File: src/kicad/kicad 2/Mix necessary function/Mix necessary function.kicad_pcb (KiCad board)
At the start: 2 copper layers, 53 x 58 mm, 22 parts, among them SW1 02-JST, SW2 02-JST

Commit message: twelite
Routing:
- net N$9: vias 1 -> 0
- net N$8: vias 1 -> 0
- net N$7: vias 1 -> 0
- net N$6: vias 1 -> 0
- net N$5: vias 1 -> 0
- net N$4: vias 1 -> 0
- net N$3: vias 1 -> 0
- net N$18: vias 1 -> 0
- net N$17: vias 1 -> 0
- net N$16: vias 1 -> 0
- net N$15: vias 1 -> 0
- net N$14: vias 1 -> 0
- net N$12: vias 1 -> 0
- net N$11: vias 1 -> 0
- net N$10: vias 1 -> 0
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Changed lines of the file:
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@@
       (outputformat 1)
       (mirror false)
-      (drillshape 1)
+      (drillshape 0)
       (scaleselection 1)
-      (outputdirectory "")
+      (outputdirectory "gerber/")
     )
   )
@@
   (net 9 "PWM2_SERVO")
   (net 10 "PWM1_SERVO")
-  (net 11 "N$1")
-  (net 12 "N$3")
-  (net 13 "N$4")
-  (net 14 "N$5")
-  (net 15 "N$6")
-  (net 16 "N$7")
-  (net 17 "N$8")
-  (net 18 "N$9")
-  (net 19 "N$10")
-  (net 20 "N$11")
-  (net 21 "N$12")
-  (net 22 "N$13")
-  (net 23 "N$14")
-  (net 24 "N$15")
-  (net 25 "N$16")
-  (net 26 "N$17")
-  (net 27 "N$18")
+  (net 11 "N$13")
   (footprint "Mix necessary function:ＮＪＭ７８０６ＦＡ-6V" (layer "F.Cu")
     (at 155.0011 100.0036 90)
@@
     (fp_line (start 10.65 -8) (end 10.65 -3.9)
       (stroke (width 0.127) (type solid)) (layer "F.SilkS"))
-    (fp_arc (start -7 2.6) (mid -9.398063 -0.328203) (end -10.65 -3.9)
+    (fp_arc (start -7 2.6) (mid -9.398061 -0.328204) (end -10.65 -3.9)
       (stroke (width 0.127) (type solid)) (layer "F.SilkS"))
     (fp_arc (start 10.65 -3.9) (mid 9.398063 -0.328203) (end 7 2.6)
@@
   (segment (start 159.145781 107.1932) (end 160.2911 108.338519) (width 0.5) (layer "F.Cu") (net 1))
   (segment (start 160.4311 120.2936) (end 160.2911 120.1536) (width 0.5) (layer "F.Cu") (net 1))
+  (via (at 137.1141 118.5266) (size 0.7564) (drill 0.35) (layers "F.Cu" "B.Cu") (net 2))
+  (via (at 169.8801 123.7336) (size 0.7564) (drill 0.35) (layers "F.Cu" "B.Cu") (net 2))
+  (via (at 155.9101 87.2216) (size 0.7564) (drill 0.35) (layers "F.Cu" "B.Cu") (net 2))
+  (via (at 144.3361 119.4146) (size 0.7564) (drill 0.35) (layers "F.Cu" "B.Cu") (net 2))
+  (via (at 162.4511 124.6066) (size 0.7564) (drill 0.35) (layers "F.Cu" "B.Cu") (net 2))
+  (via (at 146.9401 131.6406) (size 0.7564) (drill 0.35) (layers "F.Cu" "B.Cu") (free) (net 2))
+  (via (at 154.1001 107.7326) (size 0.7564) (drill 0.35) (layers "F.Cu" "B.Cu") (net 2))
+  (via (at 136.3521 131.9886) (size 0.7564) (drill 0.35) (layers "F.Cu" "B.Cu") (net 2))
+  (via (at 149.5281 107.1766) (size 0.7564) (drill 0.35) (layers "F.Cu" "B.Cu") (net 2))
+  (via (at 136.4791 123.2256) (size 0.7564) (drill 0.35) (layers "F.Cu" "B.Cu") (net 2))
+  (via (at 150.9251 99.5566) (size 0.7564) (drill 0.35) (layers "F.Cu" "B.Cu") (net 2))
+  (via (at 138.6541 97.9206) (size 0.7564) (drill 0.35) (layers "F.Cu" "B.Cu") (net 2))
+  (via (at 167.3401 87.2216) (size 0.7564) (drill 0.35) (layers "F.Cu" "B.Cu") (net 2))
+  (via (at 158.8781 104.1446) (size 0.7564) (drill 0.35) (layers "F.Cu" "B.Cu") (net 2))
+  (via (at 148.0191 123.2246) (size 0.7564) (drill 0.35) (layers "F.Cu" "B.Cu") (net 2))
+  (via (at 163.0221 131.2266) (size 0.7564) (drill 0.35) (layers "F.Cu" "B.Cu") (net 2))
   (segment (start 165.1511 99.5736) (end 165.1511 90.1436) (width 1.016) (layer "F.Cu") (net 3))
   (segment (start 156.503556 88.4752) (end 166.482968 88.4752) (width 1.016) (layer "F.Cu") (net 4))
@@
   (segment (start 135.4611 129.0036) (end 135.4611 129.4636) (width 0.2) (layer "F.Cu") (net 10))
   (segment (start 146.0011 131.0036) (end 147.7471 129.2576) (width 0.2) (layer "F.Cu") (net 10))
-  (via (at 148.0191 123.2246) (size 0.7564) (drill 0.35) (layers "F.Cu" "B.Cu") (net 11))
-  (via (at 146.9401 131.6406) (size 0.7564) (drill 0.35) (layers "F.Cu" "B.Cu") (net 12))
-  (via (at 137.1141 118.5266) (size 0.7564) (drill 0.35) (layers "F.Cu" "B.Cu") (net 13))
-  (via (at 144.3361 119.4146) (size 0.7564) (drill 0.35) (layers "F.Cu" "B.Cu") (net 14))
-  (via (at 136.3521 131.9886) (size 0.7564) (drill 0.35) (layers "F.Cu" "B.Cu") (net 15))
-  (via (at 136.4791 123.2256) (size 0.7564) (drill 0.35) (layers "F.Cu" "B.Cu") (net 16))
-  (via (at 154.1001 107.7326) (size 0.7564) (drill 0.35) (layers "F.Cu" "B.Cu") (net 17))
-  (via (at 149.5281 107.1766) (size 0.7564) (drill 0.35) (layers "F.Cu" "B.Cu") (net 18))
-  (via (at 158.8781 104.1446) (size 0.7564) (drill 0.35) (layers "F.Cu" "B.Cu") (net 19))
-  (via (at 150.9251 99.5566) (size 0.7564) (drill 0.35) (layers "F.Cu" "B.Cu") (net 20))
-  (via (at 138.6541 97.9206) (size 0.7564) (drill 0.35) (layers "F.Cu" "B.Cu") (net 21))
-  (via (at 162.5141 118.9076) (size 0.7564) (drill 0.35) (layers "F.Cu" "B.Cu") (net 22))
-  (via (at 162.4511 124.6066) (size 0.7564) (drill 0.35) (layers "F.Cu" "B.Cu") (net 23))
-  (via (at 169.8801 123.7336) (size 0.7564) (drill 0.35) (layers "F.Cu" "B.Cu") (net 24))
-  (via (at 163.0221 131.2266) (size 0.7564) (drill 0.35) (layers "F.Cu" "B.Cu") (net 25))
-  (via (at 155.9101 87.2216) (size 0.7564) (drill 0.35) (layers "F.Cu" "B.Cu") (net 26))
-  (via (at 167.3401 87.2216) (size 0.7564) (drill 0.35) (layers "F.Cu" "B.Cu") (net 27))
+  (via (at 162.5141 118.9076) (size 0.7564) (drill 0.35) (layers "F.Cu" "B.Cu") (net 11))
   (zone (net 2) (net_name "GND") (layer "F.Cu") (hatch edge 0.5)
     (priority 6)

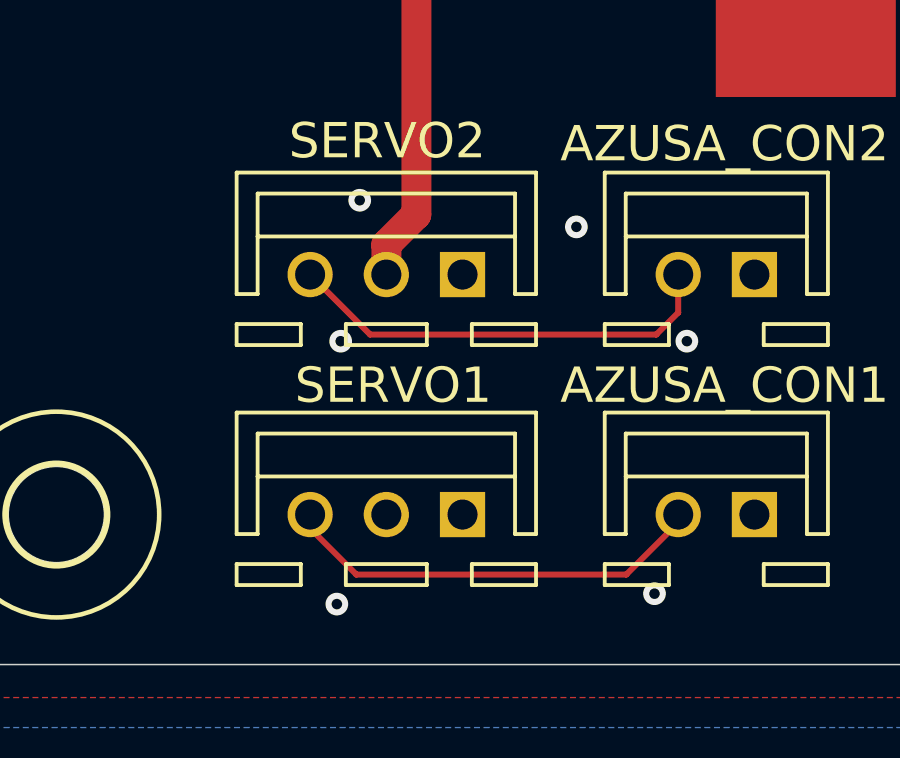
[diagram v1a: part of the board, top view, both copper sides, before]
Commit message: fix twelite circuit slot
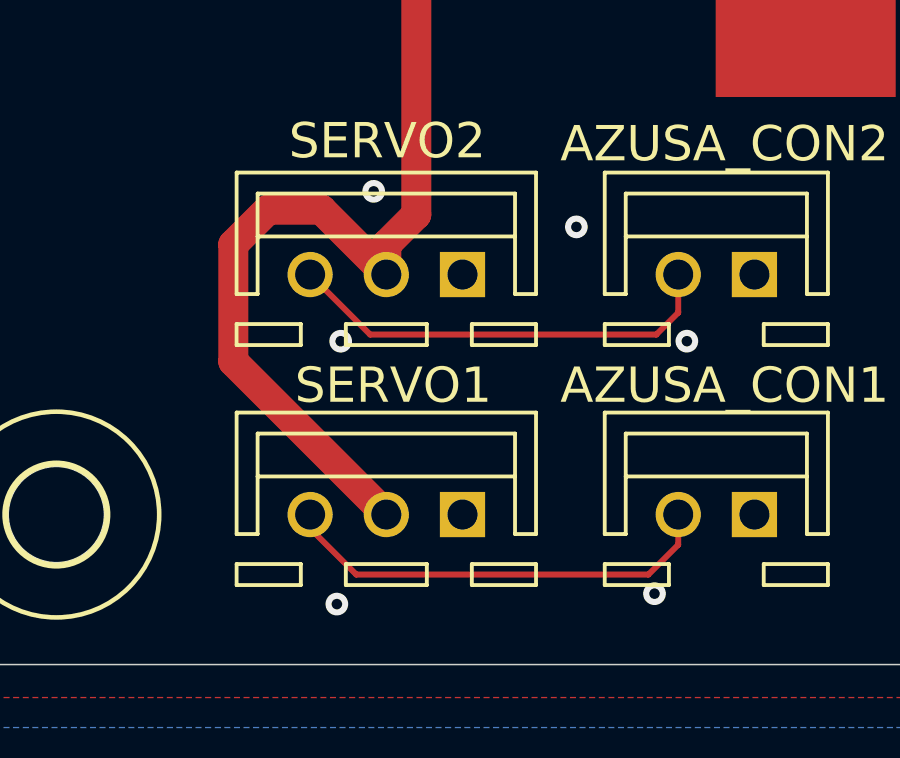
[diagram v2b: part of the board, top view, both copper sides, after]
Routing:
- net +6V: track 42.0 -> 59.6 mm
- net PWM1_SERVO: track 14.1 -> 14.8 mm
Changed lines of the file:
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@@
     (fp_line (start 10.65 -8) (end 10.65 -3.9)
       (stroke (width 0.127) (type solid)) (layer "F.SilkS"))
-    (fp_arc (start -7 2.6) (mid -9.398061 -0.328204) (end -10.65 -3.9)
+    (fp_arc (start -7 2.6) (mid -9.39806 -0.328204) (end -10.65 -3.9)
       (stroke (width 0.127) (type solid)) (layer "F.SilkS"))
     (fp_arc (start 10.65 -3.9) (mid 9.398063 -0.328203) (end 7 2.6)
@@
   (segment (start 159.145781 107.1932) (end 160.2911 108.338519) (width 0.5) (layer "F.Cu") (net 1))
   (segment (start 160.4311 120.2936) (end 160.2911 120.1536) (width 0.5) (layer "F.Cu") (net 1))
-  (via (at 137.1141 118.5266) (size 0.7564) (drill 0.35) (layers "F.Cu" "B.Cu") (net 2))
+  (via (at 137.58 118.23) (size 0.7564) (drill 0.35) (layers "F.Cu" "B.Cu") (net 2))
   (via (at 169.8801 123.7336) (size 0.7564) (drill 0.35) (layers "F.Cu" "B.Cu") (net 2))
   (via (at 155.9101 87.2216) (size 0.7564) (drill 0.35) (layers "F.Cu" "B.Cu") (net 2))
@@
   (segment (start 155.0011 97.4636) (end 155.0001 97.4646) (width 1) (layer "F.Cu") (net 6))
   (segment (start 157.5881 97.3526) (end 158.7791 97.3526) (width 0.5) (layer "F.Cu") (net 6))
+  (segment (start 134.06 118.84) (end 132.9 120) (width 1) (layer "F.Cu") (net 6))
   (segment (start 138.0011 121.0036) (end 138.0011 120.0036) (width 1) (layer "F.Cu") (net 6))
+  (segment (start 132.9 123.9025) (end 138.0011 129.0036) (width 1) (layer "F.Cu") (net 6))
+  (segment (start 135.8375 118.84) (end 134.06 118.84) (width 1) (layer "F.Cu") (net 6))
   (segment (start 139.0011 119.0036) (end 139.0011 100.4646) (width 1) (layer "F.Cu") (net 6))
   (segment (start 157.5155 97.4252) (end 155.0395 97.4252) (width 0.5) (layer "F.Cu") (net 6))
   (segment (start 157.5155 97.4252) (end 157.5881 97.3526) (width 0.5) (layer "F.Cu") (net 6))
+  (segment (start 138.0011 121.0036) (end 135.8375 118.84) (width 1) (layer "F.Cu") (net 6))
   (segment (start 142.0011 97.4646) (end 155.0001 97.4646) (width 1) (layer "F.Cu") (net 6))
+  (segment (start 132.9 120) (end 132.9 123.9025) (width 1) (layer "F.Cu") (net 6))
   (segment (start 155.0011 97.4636) (end 155.0395 97.4252) (width 0.5) (layer "F.Cu") (net 6))
   (segment (start 139.0011 100.4646) (end 142.0011 97.4646) (width 1) (layer "F.Cu") (net 6))
@@
   (segment (start 147.7311 122.2736) (end 147.7311 121.0036) (width 0.2) (layer "F.Cu") (net 9))
   (segment (start 137.4611 123.0036) (end 147.0011 123.0036) (width 0.2) (layer "F.Cu") (net 9))
-  (segment (start 137.0011 131.0036) (end 146.0011 131.0036) (width 0.2) (layer "F.Cu") (net 10))
   (segment (start 135.4611 129.4636) (end 137.0011 131.0036) (width 0.2) (layer "F.Cu") (net 10))
+  (segment (start 147.7311 130.0089) (end 147.7311 129.0036) (width 0.2) (layer "F.Cu") (net 10))
+  (segment (start 137.0011 131.0036) (end 146.7364 131.0036) (width 0.2) (layer "F.Cu") (net 10))
+  (segment (start 146.7364 131.0036) (end 147.7311 130.0089) (width 0.2) (layer "F.Cu") (net 10))
   (segment (start 135.4611 129.0036) (end 135.4611 129.4636) (width 0.2) (layer "F.Cu") (net 10))
-  (segment (start 146.0011 131.0036) (end 147.7471 129.2576) (width 0.2) (layer "F.Cu") (net 10))
   (via (at 162.5141 118.9076) (size 0.7564) (drill 0.35) (layers "F.Cu" "B.Cu") (net 11))
   (zone (net 2) (net_name "GND") (layer "F.Cu") (hatch edge 0.5)

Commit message: fix
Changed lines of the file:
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@@
     (fp_line (start 10.65 -8) (end 10.65 -3.9)
       (stroke (width 0.127) (type solid)) (layer "F.SilkS"))
-    (fp_arc (start -7 2.6) (mid -9.39806 -0.328204) (end -10.65 -3.9)
+    (fp_arc (start -7 2.6) (mid -9.398061 -0.328204) (end -10.65 -3.9)
       (stroke (width 0.127) (type solid)) (layer "F.SilkS"))
     (fp_arc (start 10.65 -3.9) (mid 9.398063 -0.328203) (end 7 2.6)
@@
   (segment (start 137.4611 123.0036) (end 147.0011 123.0036) (width 0.2) (layer "F.Cu") (net 9))
   (segment (start 135.4611 129.4636) (end 137.0011 131.0036) (width 0.2) (layer "F.Cu") (net 10))
-  (segment (start 147.7311 130.0089) (end 147.7311 129.0036) (width 0.2) (layer "F.Cu") (net 10))
+  (segment (start 147.7311 129.0036) (end 147.7311 130.0089) (width 0.2) (layer "F.Cu") (net 10))
   (segment (start 137.0011 131.0036) (end 146.7364 131.0036) (width 0.2) (layer "F.Cu") (net 10))
   (segment (start 146.7364 131.0036) (end 147.7311 130.0089) (width 0.2) (layer "F.Cu") (net 10))
